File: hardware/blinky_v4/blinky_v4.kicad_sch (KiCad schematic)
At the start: 155 parts, among them J1 Conn_01x07, J2 Conn_01x03_Pin, J3 RJ45, J4 Conn_01x06_Pin, J5 Conn_01x05_Pin, J6 Conn_02x10_Counter_Clockwise, J7 Conn_01x04_Pin, J8 Conn_01x04_Pin, J9 Conn_01x06_Pin, Q1 2N7002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

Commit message: add TP
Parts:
- added TP25: ~, TestPoint:TestPoint_THTPad_D1.5mm_Drill0.7mm, symbol Connector:TestPoint
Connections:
- net EXT_CLK_IN: now also TP25.1
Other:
- moved on the sheet: TP23

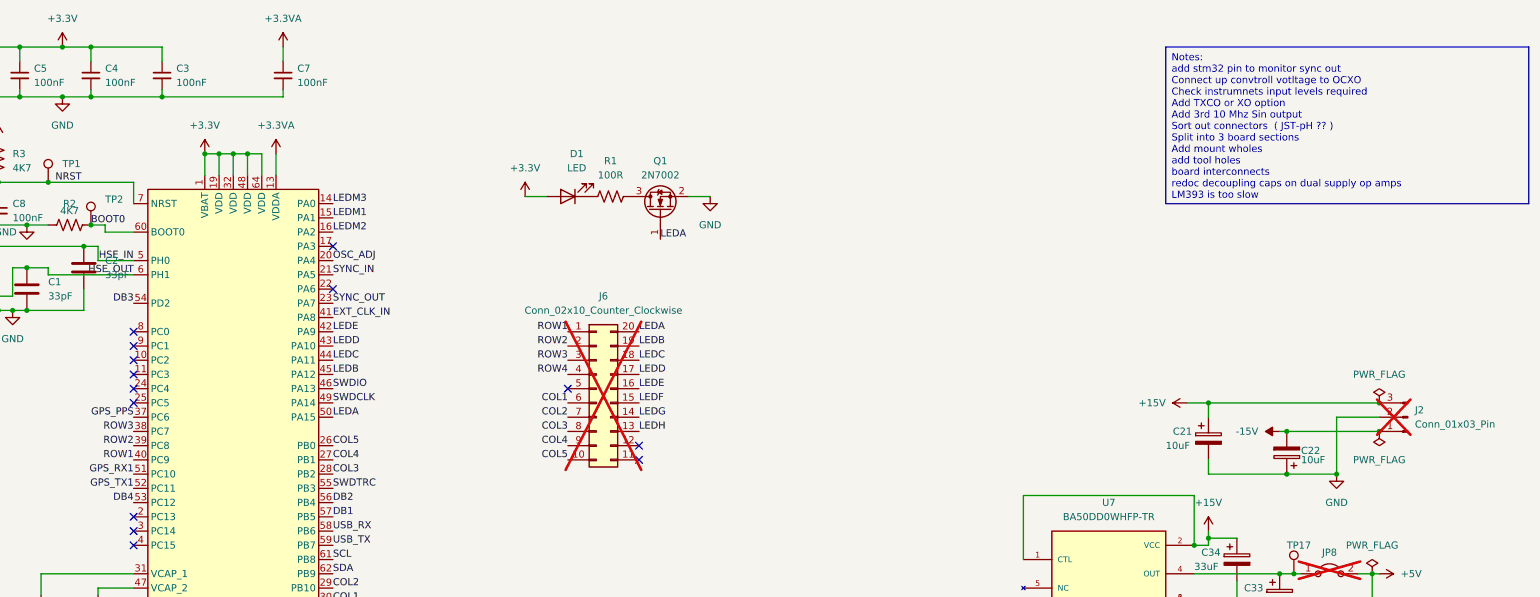
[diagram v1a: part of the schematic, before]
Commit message: move the COL3 off of BOOOT1
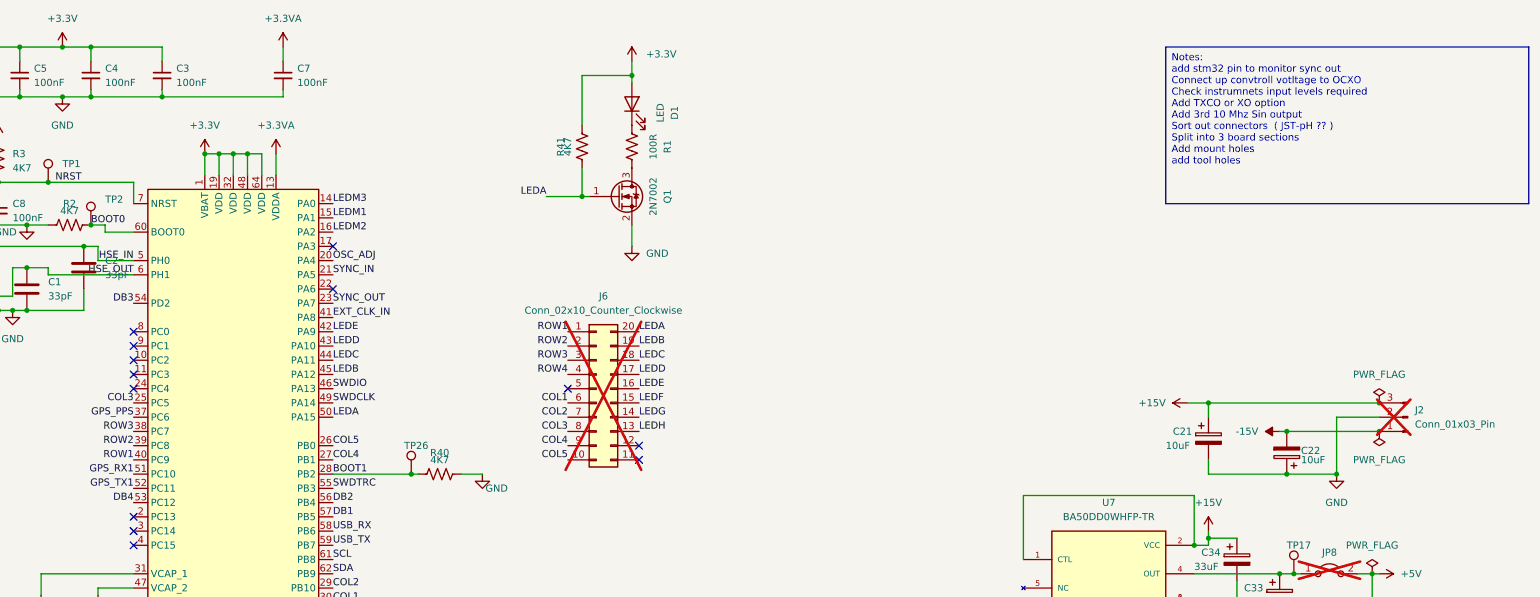
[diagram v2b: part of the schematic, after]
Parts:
- added R40, R41: 4K7, Resistor_SMD:R_0603_1608Metric, symbol Device:R_US
- added TP26: ~, TestPoint:TestPoint_THTPad_D1.5mm_Drill0.7mm, symbol Connector:TestPoint
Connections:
- net +3.3V: now also R41.1
- net COL3: now also U1.25 (PC5); no longer U1.28 (PB2)
- net GND: now also R40.1
- net LEDA: now also R41.2
- new net BOOT1: R40.2, TP26.1, U1.28 (PB2)
- no-connect marks 14 -> 13
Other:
- moved on the sheet: D1, Q1, R1

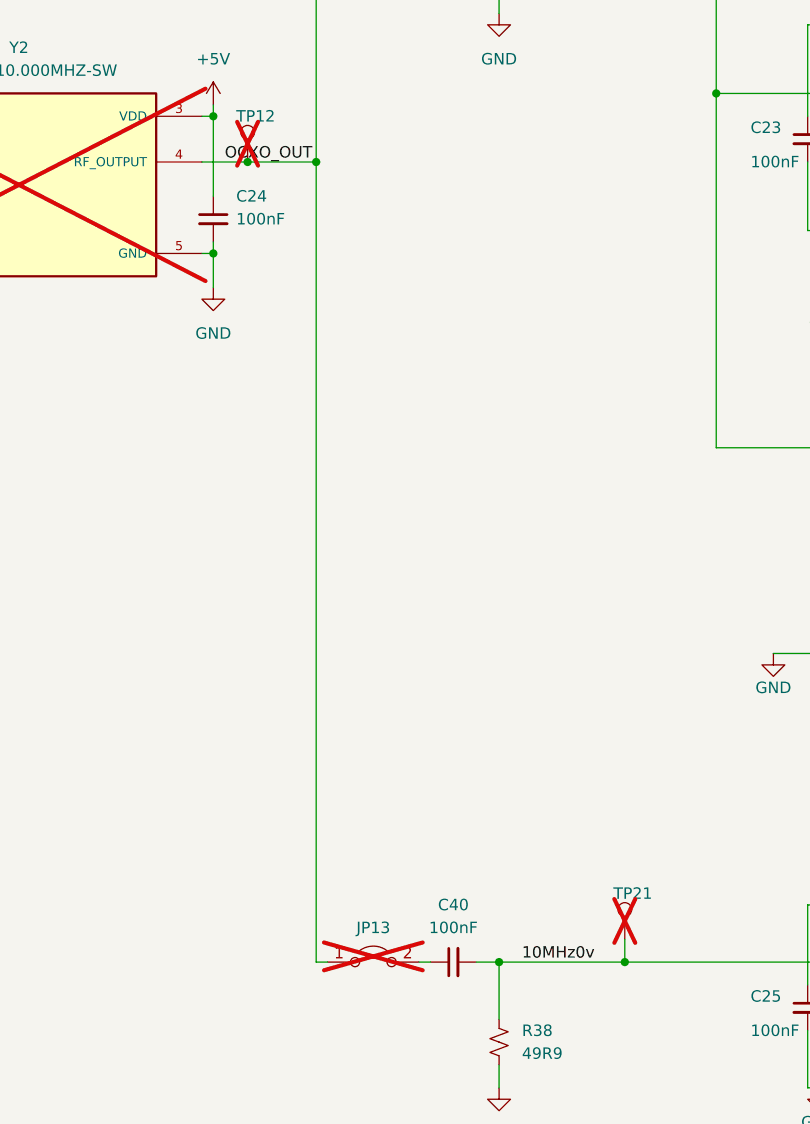
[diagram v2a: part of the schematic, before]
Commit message: add ext 10Mhz in BNC
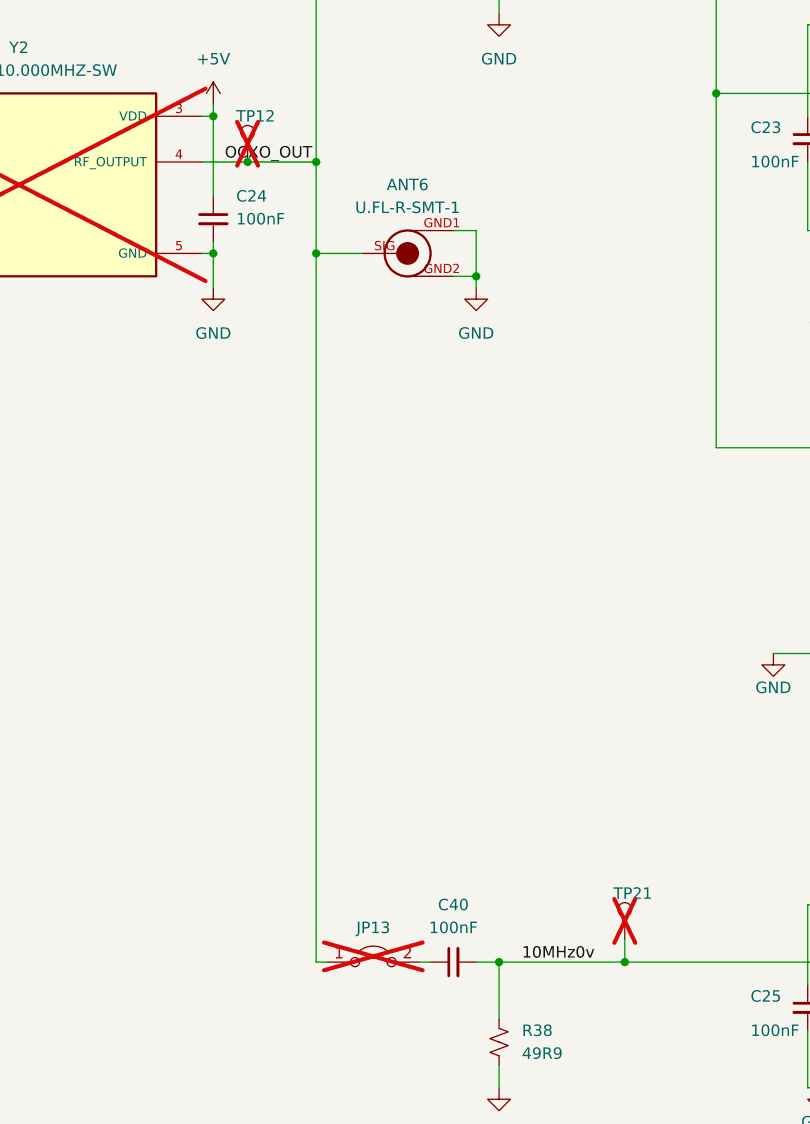
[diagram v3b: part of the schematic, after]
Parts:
- added ANT6: U.FL-R-SMT-1, blinky_footprints:U.FL-R-SMT-1, symbol blinky:U.FL-R-SMT-1
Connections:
- net GND: now also ANT6.GND1, ANT6.GND2
- net OCXO_OUT: now also ANT6.SIG
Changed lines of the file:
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@@
   (junction (at 267.97 63.5) (diameter 0) (color 0 0 0 0)
   )
+  (junction (at 96.52 269.24) (diameter 0) (color 0 0 0 0)
+  )
   (junction (at 172.72 222.25) (diameter 0) (color 0 0 0 0)
   )
@@
   (junction (at 175.26 199.39) (diameter 0) (color 0 0 0 0)
   )
+  (junction (at 114.3 271.78) (diameter 0) (color 0 0 0 0)
+  )
   (junction (at 257.81 59.69) (diameter 0) (color 0 0 0 0)
   )
@@
     (stroke (width 0) (type default))
   )
-  (wire (pts (xy 96.52 347.98) (xy 96.52 259.08))
+  (wire (pts (xy 96.52 347.98) (xy 96.52 269.24))
     (stroke (width 0) (type default))
   )
@@
     (stroke (width 0) (type default))
   )
+  (wire (pts (xy 111.76 271.78) (xy 114.3 271.78))
+    (stroke (width 0) (type default))
+  )
   (wire (pts (xy 245.11 36.83) (xy 256.54 36.83))
     (stroke (width 0) (type default))
@@
     (stroke (width 0) (type default))
   )
+  (wire (pts (xy 96.52 269.24) (xy 101.6 269.24))
+    (stroke (width 0) (type default))
+  )
   (wire (pts (xy 448.31 271.78) (xy 448.31 275.59))
     (stroke (width 0) (type default))
@@
     (stroke (width 0) (type default))
   )
+  (wire (pts (xy 96.52 269.24) (xy 96.52 259.08))
+    (stroke (width 0) (type default))
+  )
   (wire (pts (xy 242.57 67.31) (xy 242.57 74.93))
     (stroke (width 0) (type default))
@@
     (stroke (width 0) (type default))
   )
+  (wire (pts (xy 114.3 266.7) (xy 111.76 266.7))
+    (stroke (width 0) (type default))
+  )
   (wire (pts (xy 163.83 256.54) (xy 165.1 256.54))
     (stroke (width 0) (type default))
@@
     (stroke (width 0) (type default))
   )
+  (wire (pts (xy 114.3 271.78) (xy 114.3 266.7))
+    (stroke (width 0) (type default))
+  )
   (wire (pts (xy 448.31 261.62) (xy 448.31 255.27))
     (stroke (width 0) (type default))
@@
     (stroke (width 0) (type default))
   )
+  (wire (pts (xy 114.3 273.05) (xy 114.3 271.78))
+    (stroke (width 0) (type default))
+  )
   (wire (pts (xy 165.1 341.63) (xy 165.1 342.9))
     (stroke (width 0) (type default))
@@
     )
   )
+  (symbol (lib_id "power:GND") (at 114.3 273.05 0) (unit 1)
+    (in_bom yes) (on_board yes) (dnp no) (fields_autoplaced)
+    (property "Reference" "#PWR084" (at 114.3 279.4 0)
+      (effects (font (size 1.27 1.27)) hide)
+    )
+    (property "Value" "GND" (at 114.3 278.13 0)
+      (effects (font (size 1.27 1.27)))
+    )
+    (property "Footprint" "" (at 114.3 273.05 0)
+      (effects (font (size 1.27 1.27)) hide)
+    )
+    (property "Datasheet" "" (at 114.3 273.05 0)
+      (effects (font (size 1.27 1.27)) hide)
+    )
+    (pin "1")
+    (instances
+      (project "blinky_v4"
+        (path "/bd4d3b9a-07c1-4a53-9c94-2893f3e869d4"
+          (reference "#PWR084") (unit 1)
+        )
+      )
+    )
+  )
   (symbol (lib_id "power:GND") (at 339.09 104.14 0) (unit 1)
     (in_bom yes) (on_board yes) (dnp no)
@@
         )
       )
+    )
+  )
+  (symbol (lib_id "blinky:U.FL-R-SMT-1") (at 106.68 269.24 0) (unit 1)
+    (in_bom yes) (on_board yes) (dnp no) (fields_autoplaced)
+    (property "Reference" "ANT6" (at 106.68 261.62 0)
+      (effects (font (size 1.27 1.27)))
+    )
+    (property "Value" "U.FL-R-SMT-1" (at 106.68 264.16 0)
+      (effects (font (size 1.27 1.27)))
+    )
+    (property "Footprint" "blinky_footprints:U.FL-R-SMT-1" (at 106.68 269.24 0)
+      (effects (font (size 1.27 1.27)) (justify bottom) hide)
+    )
+    (property "Datasheet" "https://jlcpcb.com/partdetail/hrs_hirose-U_FL_R_SMT_1_80/C88374#:~:text=Datasheet-,Download,-Source" (at 106.68 269.24 0)
+      (effects (font (size 1.27 1.27)) hide)
+    )
+    (property "LCSC" "C88374" (at 106.68 269.24 0)
+      (effects (font (size 1.27 1.27)) hide)
+    )
+    (pin "GND1")
+    (pin "GND2")
+    (pin "SIG")
+    (instances
+      (project "blinky_v4"
+        (path "/bd4d3b9a-07c1-4a53-9c94-2893f3e869d4"
+          (reference "ANT6") (unit 1)
+        )
+      )

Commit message: starting updates for V4
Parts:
- added C? (x2): 150pF, Capacitor_SMD:C_0603_1608Metric, symbol Device:C_Small
- added C?: 330pF, Capacitor_SMD:C_0201_0603Metric, symbol Device:C_Small
- added C?: 220pF, Capacitor_SMD:C_0201_0603Metric, symbol Device:C_Small
- added L? (x2): 1uF, Inductor_SMD:L_0805_2012Metric, symbol Device:L_Small
- C12: value 100nF -> 1.5nF; LCSC C14663 -> C1595
- R13, R30: now not fitted
- U3, U8, U9: now not fitted; now left out of the parts list
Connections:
- net GND: now also C?.1, C?.2, C?.2, C?.2
- new net: C?.1, L?.1
- new net: C?.1, C?.1, L?.2, L?.2
- new net: C?.2, L?.1
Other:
- note added: "12 MHz 5th Order Butterworth Lowpass"

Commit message: updates for output filter
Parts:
- C43, C44: renamed from C?; footprint Capacitor_SMD:C_0201_0603Metric -> Capacitor_SMD:C_0603_1608Metric
- gave numbers to parts that had none: 4
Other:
- moved on the sheet: TP10, TP9

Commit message: update
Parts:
- U2: now not fitted; now left out of the parts list
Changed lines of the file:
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@@
   )
   (symbol (lib_id "Amplifier_Operational:ADA4807-1") (at 167.64 350.52 0) (unit 1)
-    (in_bom yes) (on_board yes) (dnp no)
+    (in_bom no) (on_board yes) (dnp yes)
     (property "Reference" "U2" (at 167.64 344.17 0)
       (effects (font (size 1.27 1.27)))

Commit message: update voltages for req adj
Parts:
- added C?: 100nF, Capacitor_SMD:C_0402_1005Metric, symbol Device:C_Small
- added JP? (x2): SolderJumper_2_Bridged, Jumper:SolderJumper-2_P1.3mm_Bridged_RoundedPad1.0x1.5mm, symbol Jumper:SolderJumper_2_Bridged
- added R?: 1K0, Resistor_SMD:R_0603_1608Metric, symbol Device:R_Small_US
- C16, C18, C22, C40: now not fitted; now left out of the parts list
- R18: value 49R9 -> 2R; LCSC C17720 -> C17606
- R19: value 1K0 -> 270R; LCSC C21190 -> C17590
- R20, R21: value 1K0 -> 1K5; LCSC C21190 -> C4310
- R22: value 1K0 -> 330R; LCSC C21190 -> C17630
- R23: value 49R9 -> 20R; LCSC C17720 -> C17544
- R24: value 49R9 -> 22K; LCSC C17720 -> C17560
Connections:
- net GND: now also C?.2
- net OSC_ADJ: now also R?.2; no longer R24.1
- net at J5.4 (Pin_4), R20.2, R21.1: now also JP?.1 (A)
- net at J5.3 (Pin_3), Y2.1 (VC): now also JP?.1 (A), JP?.2 (B)
- net at J5.2 (Pin_2): now also R24.1, C?.1, R?.1; no longer R24.2
- new net: JP?.2 (B), R24.2
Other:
- moved on the sheet: C36, C43, C44, C45, J5, L1, L2, R24

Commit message: start PCB update
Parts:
- R26, R5: now not fitted; now left out of the parts list
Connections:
- net at C36.1, L1.1: now also C9.1
- net at ANT1.SIG: now also C45.2, L2.1; no longer C9.1
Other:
- moved on the sheet: ANT1, C36, C43, C44, C45, L1, L2
